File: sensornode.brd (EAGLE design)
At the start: 112.3 x 61 mm, 73 parts, among them IC1 CP2104, Q1 mmbt2222, Q2 mmbt2222, Q3 DMG3415U, SW2 KMR2, U1 TSL2591, U2 AP2112-3.3, U3 MCP73831T-2ACI/OT, U4 BMEx80, X2 ESP32_WROOM32_SKINNY, X4 20329

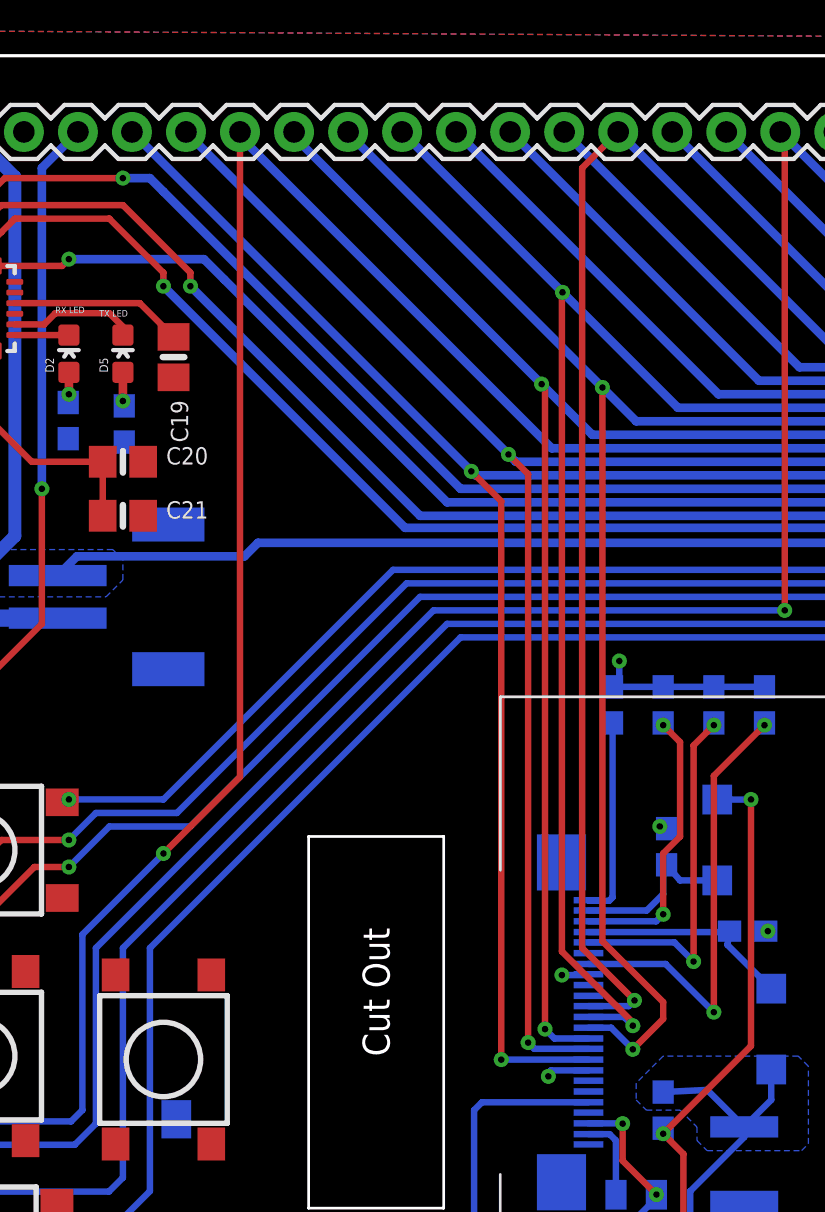
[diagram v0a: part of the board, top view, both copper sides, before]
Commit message: Moving vias out from under FPC connector
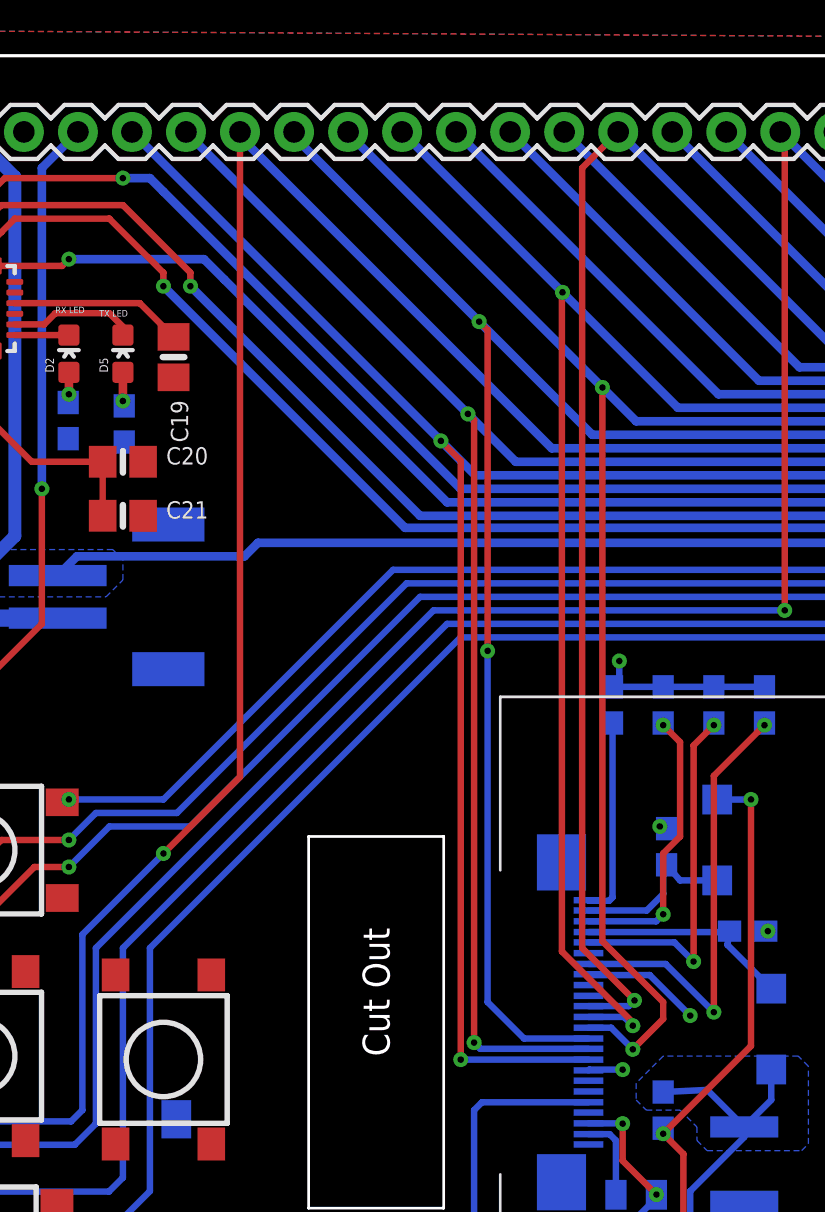
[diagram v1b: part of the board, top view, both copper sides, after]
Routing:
- net EINK_DC_IO17: track 107.8 -> 112.8 mm
- net EINK_RESET_IO16: track 109.0 -> 113.2 mm
- net GND: track 26.6 -> 30.5 mm
- net EINK_BUSY_A5_IO4: track 111.5 -> 114.6 mm
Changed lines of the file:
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@@
 <wire x1="49.2075" y1="2.54" x2="49.2075" y2="5.075" width="0.3048" layer="16"/>
 <wire x1="49.2075" y1="5.075" x2="49.2125" y2="5.08" width="0.3048" layer="16"/>
-<wire x1="40.93845" y1="13.2969" x2="39.17315" y2="13.2969" width="0.3048" layer="16"/>
-<wire x1="39.17315" y1="13.2969" x2="39.0525" y2="13.0175" width="0.3048" layer="16"/>
-<via x="39.0525" y="13.0175" extent="1-16" drill="0.3048"/>
 <wire x1="37.25" y1="5.08" x2="37.1475" y2="5.08" width="0.3048" layer="16"/>
 <via x="37.1475" y="5.08" extent="1-16" drill="0.3048"/>
@@
 <wire x1="37.1475" y1="2.6425" x2="37.25" y2="2.54" width="0.3048" layer="16"/>
 <wire x1="40.93845" y1="17.8181" x2="40.90035" y2="17.78" width="0.3048" layer="16"/>
-<wire x1="40.90035" y1="17.78" x2="39.6875" y2="17.78" width="0.3048" layer="16"/>
-<via x="39.6875" y="17.78" extent="1-16" drill="0.3048"/>
 <wire x1="42.38625" y1="32.54375" x2="42.38625" y2="31.6475" width="0.3048" layer="16"/>
 <wire x1="42.38625" y1="31.6475" x2="42.06875" y2="31.33" width="0.3048" layer="16"/>
@@
 <vertex x="6.35" y="17.78"/>
 </polygon>
+<wire x1="40.93845" y1="13.2969" x2="40.97655" y2="13.335" width="0.3048" layer="16"/>
+<wire x1="40.97655" y1="13.335" x2="42.545" y2="13.335" width="0.3048" layer="16"/>
+<via x="42.545" y="13.335" extent="1-16" drill="0.3048"/>
+<wire x1="40.90035" y1="17.78" x2="43.815" y2="17.78" width="0.3048" layer="16"/>
+<wire x1="43.815" y1="17.78" x2="45.72" y2="15.875" width="0.3048" layer="16"/>
+<via x="45.72" y="15.875" extent="1-16" drill="0.3048"/>
 <wire x1="96.995" y1="44.4275" x2="94.615" y2="43.18" width="0" layer="19" extent="1-1"/>
 </signal>
@@
 <wire x1="21.9075" y1="57.30875" x2="22.015" y2="57.41625" width="0.4064" layer="16"/>
 <contactref element="U$15" pad="10-RES#"/>
-<wire x1="22.015" y1="57.41625" x2="37.175625" y2="42.255625" width="0.4064" layer="16"/>
-<wire x1="37.175625" y1="42.255625" x2="37.52125" y2="41.91" width="0.4064" layer="16"/>
-<wire x1="40.93845" y1="14.3129" x2="38.3921" y2="14.3129" width="0.3048" layer="16"/>
-<wire x1="38.3921" y1="14.3129" x2="38.1" y2="14.605" width="0.3048" layer="16"/>
-<via x="38.1" y="14.605" extent="1-16" drill="0.3048"/>
-<wire x1="38.1" y1="14.605" x2="38.1" y2="41.33125" width="0.3048" layer="1"/>
-<wire x1="38.1" y1="41.33125" x2="37.175625" y2="42.255625" width="0.3048" layer="1"/>
-<via x="37.175625" y="42.255625" extent="1-16" drill="0.3048"/>
+<wire x1="22.015" y1="57.41625" x2="35.270625" y2="44.160625" width="0.4064" layer="16"/>
+<wire x1="35.270625" y1="44.160625" x2="37.52125" y2="41.91" width="0.4064" layer="16"/>
+<wire x1="40.93845" y1="14.3129" x2="35.8521" y2="14.3129" width="0.3048" layer="16"/>
+<via x="35.56" y="14.605" extent="1-16" drill="0.3048"/>
+<wire x1="35.8521" y1="14.3129" x2="35.56" y2="14.605" width="0.3048" layer="16"/>
+<wire x1="35.56" y1="14.605" x2="35.56" y2="43.87125" width="0.3048" layer="1"/>
+<wire x1="35.56" y1="43.87125" x2="35.270625" y2="44.160625" width="0.3048" layer="1"/>
+<via x="35.270625" y="44.160625" extent="1-16" drill="0.3048"/>
 </signal>
 <signal name="EINK_DC_IO17">
@@
 <wire x1="26.9875" y1="57.30875" x2="27.095" y2="57.41625" width="0.4064" layer="16"/>
 <contactref element="U$15" pad="11-D/C#"/>
-<wire x1="26.9875" y1="57.30875" x2="38.735" y2="45.56125" width="0.4064" layer="16"/>
-<wire x1="38.735" y1="45.56125" x2="41.11625" y2="43.18" width="0.4064" layer="16"/>
-<wire x1="40.93845" y1="14.7955" x2="39.33825" y2="14.7955" width="0.3048" layer="16"/>
-<wire x1="39.33825" y1="14.7955" x2="38.89375" y2="15.24" width="0.3048" layer="16"/>
-<via x="38.89375" y="15.24" extent="1-16" drill="0.3048"/>
-<wire x1="38.89375" y1="15.24" x2="38.89375" y2="45.4025" width="0.3048" layer="1"/>
-<wire x1="38.89375" y1="45.4025" x2="38.735" y2="45.56125" width="0.3048" layer="1"/>
-<via x="38.735" y="45.56125" extent="1-16" drill="0.3048"/>
+<wire x1="26.9875" y1="57.30875" x2="35.798125" y2="48.498125" width="0.4064" layer="16"/>
+<wire x1="35.798125" y1="48.498125" x2="41.11625" y2="43.18" width="0.4064" layer="16"/>
+<wire x1="40.93845" y1="14.7955" x2="37.9095" y2="14.7955" width="0.3048" layer="16"/>
+<wire x1="37.9095" y1="14.7955" x2="36.195" y2="16.51" width="0.3048" layer="16"/>
+<wire x1="36.195" y1="16.51" x2="36.195" y2="33.02" width="0.3048" layer="16"/>
+<via x="36.195" y="33.02" extent="1-16" drill="0.3048"/>
+<wire x1="36.195" y1="33.02" x2="36.195" y2="48.10125" width="0.3048" layer="1"/>
+<wire x1="36.195" y1="48.10125" x2="35.798125" y2="48.498125" width="0.3048" layer="1"/>
+<via x="35.798125" y="48.498125" extent="1-16" drill="0.3048"/>
 </signal>
 <signal name="EINK_SCLK_MOSI">
@@
 <wire x1="80.645" y1="41.275" x2="35.61625" y2="41.275" width="0.4064" layer="16"/>
 <contactref element="U$15" pad="9-BUSY"/>
-<wire x1="19.475" y1="57.41625" x2="35.429375" y2="41.461875" width="0.4064" layer="16"/>
-<wire x1="35.429375" y1="41.461875" x2="35.61625" y2="41.275" width="0.4064" layer="16"/>
-<wire x1="40.93845" y1="13.8049" x2="36.83635" y2="13.8049" width="0.3048" layer="16"/>
-<via x="36.83635" y="13.8049" extent="1-16" drill="0.3048"/>
-<via x="35.429375" y="41.461875" extent="1-16" drill="0.3048"/>
-<wire x1="36.83635" y1="40.0549" x2="35.429375" y2="41.461875" width="0.3048" layer="1"/>
-<wire x1="36.83635" y1="40.0549" x2="36.83635" y2="13.8049" width="0.3048" layer="1"/>
+<wire x1="19.475" y1="57.41625" x2="34.000625" y2="42.890625" width="0.4064" layer="16"/>
+<wire x1="34.000625" y1="42.890625" x2="35.61625" y2="41.275" width="0.4064" layer="16"/>
+<wire x1="40.93845" y1="13.8049" x2="34.93135" y2="13.8049" width="0.3048" layer="16"/>
+<via x="34.93135" y="13.8049" extent="1-16" drill="0.3048"/>
+<wire x1="34.93135" y1="13.8049" x2="34.93135" y2="41.9599" width="0.3048" layer="1"/>
+<wire x1="34.93135" y1="41.9599" x2="34.000625" y2="42.890625" width="0.3048" layer="1"/>
+<via x="34.000625" y="42.890625" extent="1-16" drill="0.3048"/>
 </signal>
 <signal name="EINK_MOSI_IO23">

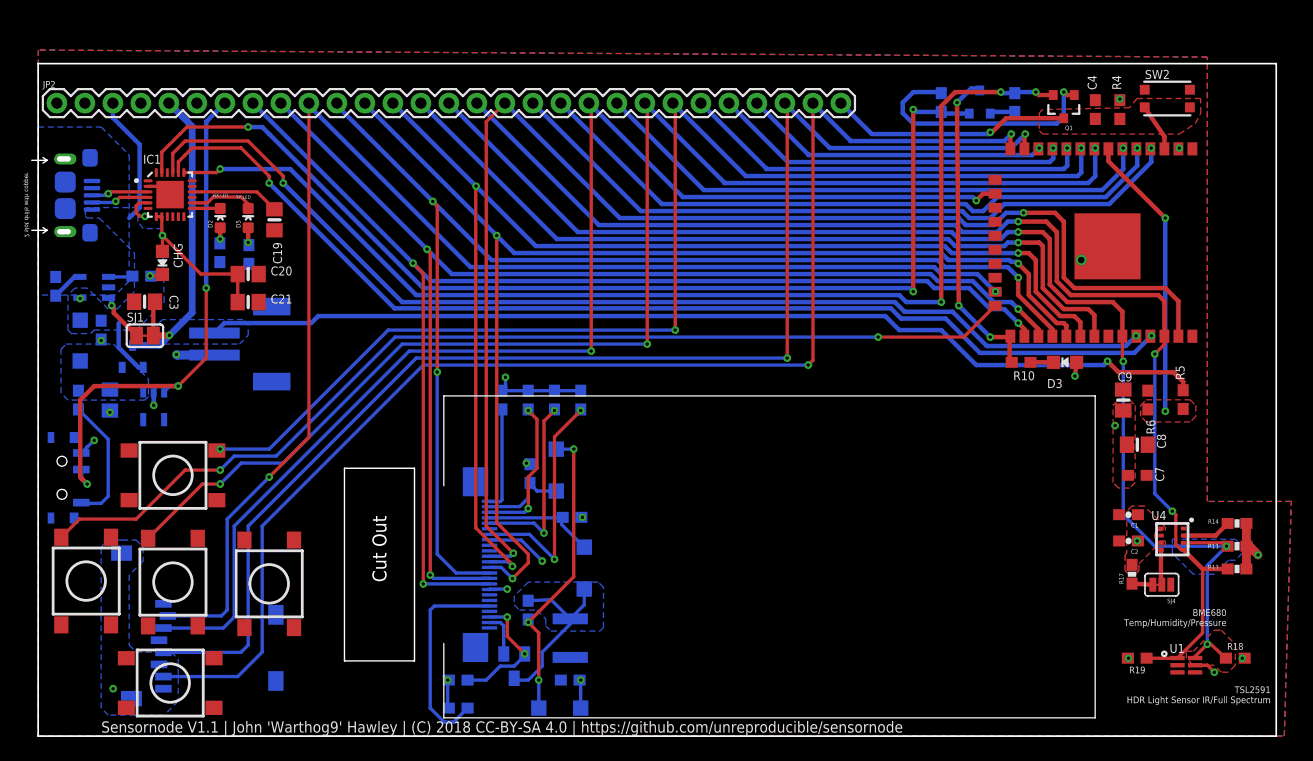
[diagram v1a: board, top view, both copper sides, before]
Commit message: Redoing the buttons
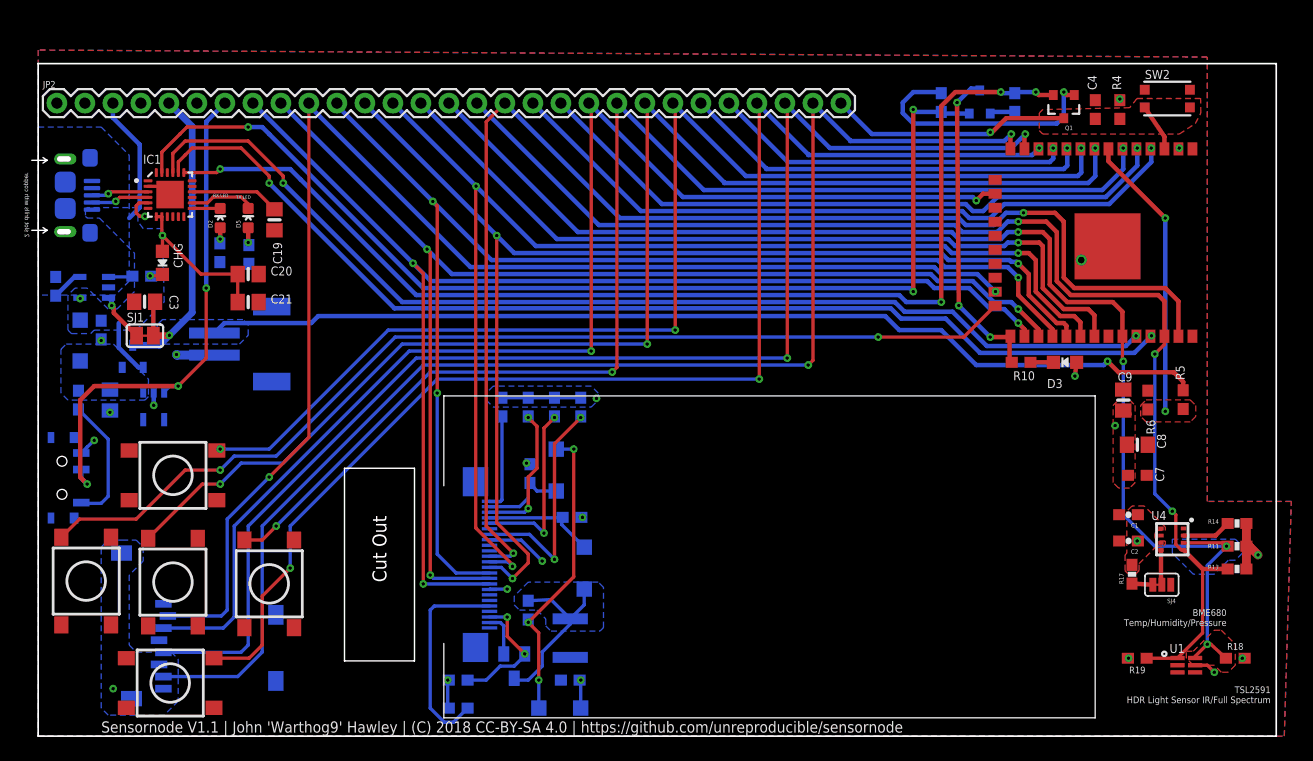
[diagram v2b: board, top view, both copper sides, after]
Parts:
- moved C15 0.64 mm to (49.2, 29.8)
- moved C16 0.64 mm to (46.8, 29.8)
- moved C17 0.64 mm to (44.5, 29.8)
- moved C18 0.64 mm to (42.1, 29.8)
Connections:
- net A13_I35 renamed BATSEN-A13_I35
- net GPIO2 renamed BTN-GPIO2
- net IO32_A7 renamed BTN-IO32_A7
- net IO33_A9 renamed BTN-IO33_A9
- removed net A2_I34: JP2.21, X2.6
- removed net IO27_A10: JP2.26, X2.12
- removed net N$21: S2.B2
- removed net N$6: S4.B2
- new net BTN-A2_I34: JP2.21, S4.B2, X2.6
- new net BTN-IO27_A10: JP2.26, S2.B2, X2.12
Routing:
- net BTN-IO27_A10: track 0.00 -> 117.9 mm, vias 0 -> 3
- net BTN-A2_I34: track 0.00 -> 116.2 mm, vias 0 -> 3
- net A2_I34: track 52.0 -> 0.00 mm, vias 1 -> 0
- net IO27_A10: track 28.0 -> 0.00 mm, vias 1 -> 0
- net GND: track 30.5 -> 29.6 mm
- net N$19: track 9.41 -> 8.77 mm
- net N$18: track 13.3 -> 12.7 mm
- net N$17: track 16.9 -> 16.3 mm
- net N$16: track 21.4 -> 20.8 mm
